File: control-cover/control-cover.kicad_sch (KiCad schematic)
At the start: 9 parts

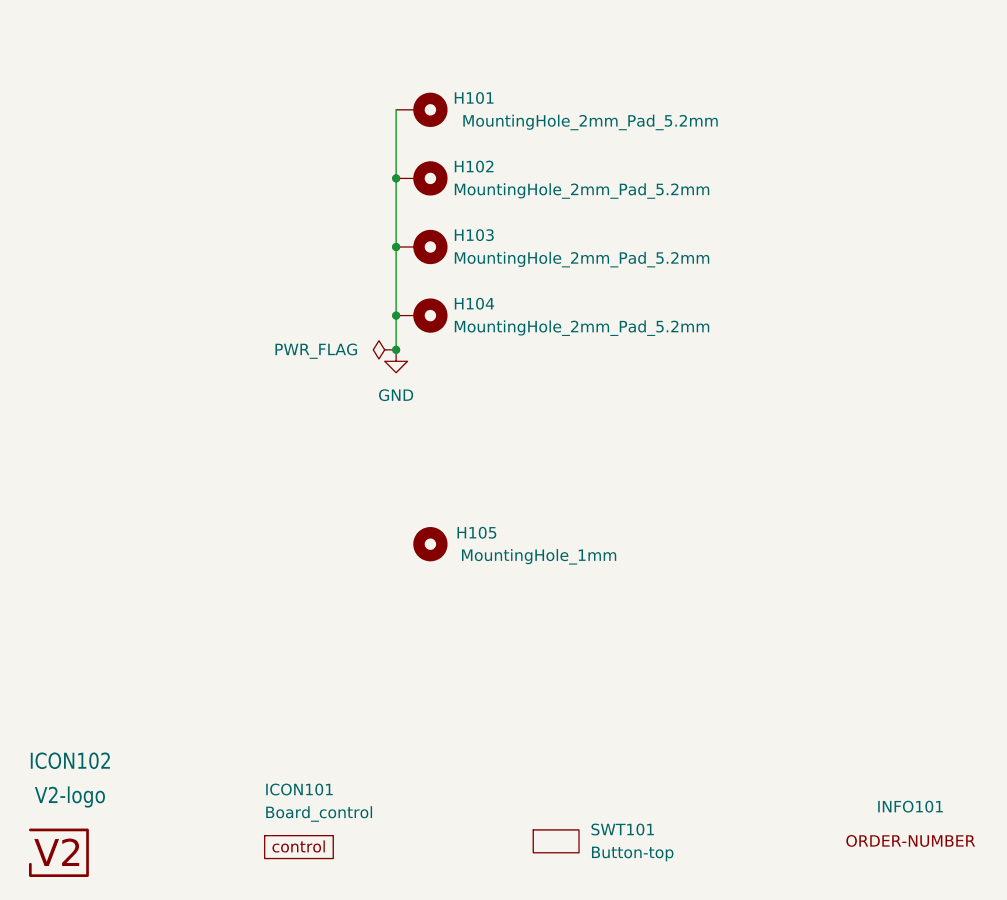
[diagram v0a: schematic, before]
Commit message: Replace Order_Number
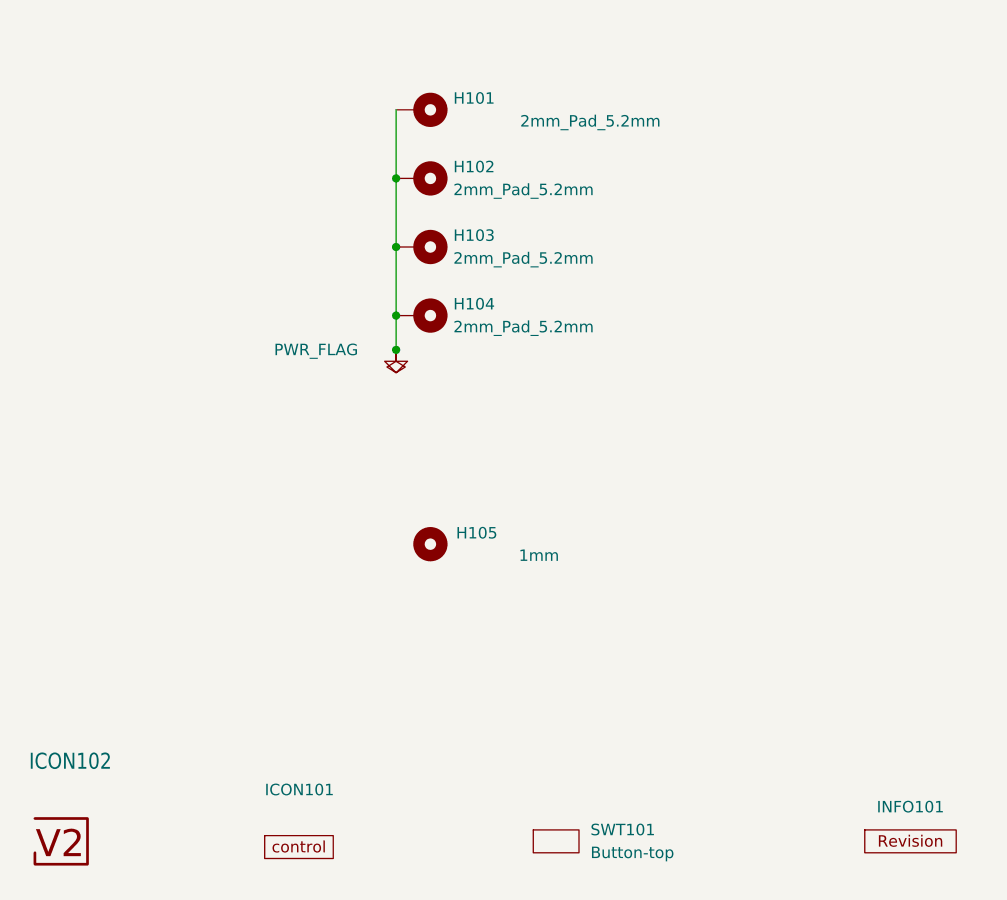
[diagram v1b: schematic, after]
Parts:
- H101, H102, H103, H104: value MountingHole_2mm_Pad_5.2mm -> 2mm_Pad_5.2mm; footprint V2_Mechanical:Mounting_Hole_2mm_Pad_5.2mm -> V2_Mechanical:MountingHole_2mm_Pad_5.2mm; now left out of the parts list
- H105: value MountingHole_1mm -> 1mm; now left out of the parts list
- INFO101: value ORDER-NUMBER -> ~; footprint V2_Production:Order_Number -> V2_Production:Revision; symbol V2_Production:Order_Number -> V2_Production:Revision
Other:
- moved on the sheet: ICON102
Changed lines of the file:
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@@
 (kicad_sch
-	(version 20231120)
+	(version 20250114)
 	(generator "eeschema")
-	(generator_version "8.0")
+	(generator_version "9.0")
 	(paper "A4")
 	(title_block
 		(title "V2 control")
-		(date "2023-01-09")
-		(rev "2")
+		(date "2026-02-13")
+		(rev "2026-02-13")
 		(company "Versio Duo")
 		(comment 1 "cover")
@@
 	)
 	(symbol
-		(lib_id "power:GND")
+		(lib_id "V2_power:GND")
 		(at 138.43 85.09 0)
 		(unit 1)
@@
 					(size 1.27 1.27)
 				)
+				(hide yes)
 			)
 		)
@@
 		(unit 1)
 		(exclude_from_sim no)
-		(in_bom yes)
+		(in_bom no)
 		(on_board yes)
 		(dnp no)
@@
 			)
 		)
-		(property "Value" "MountingHole_2mm_Pad_5.2mm"
+		(property "Value" "2mm_Pad_5.2mm"
 			(at 144.78 67.3099 90)
 			(effects
@@
 			)
 		)
-		(property "Footprint" "V2_Mechanical:Mounting_Hole_2mm_Pad_5.2mm"
+		(property "Footprint" "V2_Mechanical:MountingHole_2mm_Pad_5.2mm"
 			(at 140.97 66.04 0)
 			(effects
@@
 			)
 		)
-		(property "Description" ""
+		(property "Description" "Mounting Hole with connection"
 			(at 140.97 66.04 0)
 			(effects
@@
 	)
 	(symbol
-		(lib_id "V2_Production:Order_Number")
+		(lib_id "V2_Production:Revision")
 		(at 195.58 139.7 0)
 		(unit 1)
@@
 			)
 		)
-		(property "Value" "ORDER-NUMBER"
+		(property "Value" "~"
 			(at 195.58 142.24 0)
 			(effects
@@
 			)
 		)
-		(property "Footprint" "V2_Production:Order_Number"
+		(property "Footprint" "V2_Production:Revision"
 			(at 195.58 144.78 0)
 			(effects
@@
 			)
 		)
+		(property "Sim.Enable" "0"
+			(at 156.21 139.7 0)
+			(effects
+				(font
+					(size 1.27 1.27)
+				)
+				(hide yes)
+			)
+		)
 		(instances
 			(project "control-cover"
@@
 		(unit 1)
 		(exclude_from_sim no)
-		(in_bom yes)
+		(in_bom no)
 		(on_board yes)
 		(dnp no)
@@
 			)
 		)
-		(property "Value" "MountingHole_2mm_Pad_5.2mm"
+		(property "Value" "2mm_Pad_5.2mm"
 			(at 144.78 82.5499 90)
 			(effects
@@
 			)
 		)
-		(property "Footprint" "V2_Mechanical:Mounting_Hole_2mm_Pad_5.2mm"
+		(property "Footprint" "V2_Mechanical:MountingHole_2mm_Pad_5.2mm"
 			(at 140.97 81.28 0)
 			(effects
@@
 			)
 		)
-		(property "Description" ""
+		(property "Description" "Mounting Hole with connection"
 			(at 140.97 81.28 0)
 			(effects
@@
 	)
 	(symbol
-		(lib_name "MountingHole_2mm_Pad_5.2mm_3")
 		(lib_id "V2_Mechanical:MountingHole_2mm_Pad_5.2mm")
 		(at 140.97 58.42 270)
 		(unit 1)
 		(exclude_from_sim no)
-		(in_bom yes)
+		(in_bom no)
 		(on_board yes)
 		(dnp no)
@@
 			)
 		)
-		(property "Value" "MountingHole_2mm_Pad_5.2mm"
+		(property "Value" "2mm_Pad_5.2mm"
 			(at 160.02 59.6899 90)
 			(effects
@@
 			)
 		)
-		(property "Footprint" "V2_Mechanical:Mounting_Hole_2mm_Pad_5.2mm"
+		(property "Footprint" "V2_Mechanical:MountingHole_2mm_Pad_5.2mm"
 			(at 140.97 58.42 0)
 			(effects
@@
 			)
 		)
-		(property "Description" ""
+		(property "Description" "Mounting Hole with connection"
 			(at 140.97 58.42 0)
 			(effects
@@
 				)
 				(justify left)
+				(hide yes)
 			)
 		)
@@
 			)
 		)
+		(property "Sim.Enable" "0"
+			(at 127.635 140.335 0)
+			(effects
+				(font
+					(size 1.27 1.27)
+				)
+				(hide yes)
+			)
+		)
 		(instances
 			(project "control-cover"
@@
 	)
 	(symbol
-		(lib_id "power:PWR_FLAG")
+		(lib_id "V2_power:PWR_FLAG")
 		(at 138.43 85.09 90)
 		(unit 1)
@@
 			)
 		)
-		(property "Datasheet" "~"
+		(property "Datasheet" ""
 			(at 138.43 85.09 0)
 			(effects
@@
 			)
 		)
-		(property "Description" ""
+		(property "Description" "Special symbol for telling ERC where power comes from"
 			(at 138.43 85.09 0)
 			(effects
@@
 		(unit 1)
 		(exclude_from_sim no)
-		(in_bom yes)
+		(in_bom no)
 		(on_board yes)
 		(dnp no)
@@
 			)
 		)
-		(property "Value" "MountingHole_1mm"
+		(property "Value" "1mm"
 			(at 154.305 107.95 0)
 			(effects
@@
 			)
 		)
-		(property "Description" ""
+		(property "Description" "Mounting Hole without connection"
 			(at 142.24 106.68 0)
 			(effects
@@
 					(size 1.778 1.5113)
 				)
+				(hide yes)
 			)
 		)
@@
 		(unit 1)
 		(exclude_from_sim no)
-		(in_bom yes)
+		(in_bom no)
 		(on_board yes)
 		(dnp no)
@@
 			)
 		)
-		(property "Value" "MountingHole_2mm_Pad_5.2mm"
+		(property "Value" "2mm_Pad_5.2mm"
 			(at 144.78 74.9299 90)
 			(effects
@@
 			)
 		)
-		(property "Footprint" "V2_Mechanical:Mounting_Hole_2mm_Pad_5.2mm"
+		(property "Footprint" "V2_Mechanical:MountingHole_2mm_Pad_5.2mm"
 			(at 140.97 73.66 0)
 			(effects
@@
 			)
 		)
-		(property "Description" ""
+		(property "Description" "Mounting Hole with connection"
 			(at 140.97 73.66 0)
 			(effects
@@
 		)
 	)
+	(embedded_fonts no)
 )

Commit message: Update Library
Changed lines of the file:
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@@
-	)
-	(junction
-		(at 138.43 85.09)
-		(diameter 0)
-		(color 0 0 0 0)
 	)
 	(junction
@@
 	(symbol
 		(lib_id "V2_power:GND")
+		(at 149.86 49.53 90)
+		(unit 1)
+		(exclude_from_sim no)
+		(in_bom yes)
+		(on_board yes)
+		(dnp no)
+		(fields_autoplaced yes)
+		(property "Reference" "#PWR0102"
+			(at 156.21 49.53 0)
+			(effects
+				(font
+					(size 1.27 1.27)
+				)
+				(hide yes)
+			)
+		)
+		(property "Value" "GND"
+			(at 154.94 49.53 0)
+			(effects
+				(font
+					(size 1.27 1.27)
+				)
+				(hide yes)
+			)
+		)
+		(property "Footprint" ""
+			(at 149.86 49.53 0)
+			(effects
+				(font
+					(size 1.27 1.27)
+				)
+				(hide yes)
+			)
+		)
+		(property "Datasheet" ""
+			(at 149.86 49.53 0)
+			(effects
+				(font
+					(size 1.27 1.27)
+				)
+				(hide yes)
+			)
+		)
+		(property "Description" ""
+			(at 149.86 49.53 0)
+			(effects
+				(font
+					(size 1.27 1.27)
+				)
+				(hide yes)
+			)
+		)
+		(pin "1"
+		)
+		(instances
+			(project "control-cover"
+				(path "/6c8448b4-b04d-47e1-934e-e40cbe27a7be"
+					(reference "#PWR0102")
+					(unit 1)
+				)
+			)
+		)
+	)
+	(symbol
+		(lib_id "V2_power:GND")
 		(at 138.43 85.09 0)
 		(unit 1)
@@
 		(dnp no)
 		(fields_autoplaced yes)
-		(property "Reference" "#PWR0101"
+		(property "Reference" "#PWR101"
 			(at 138.43 91.44 0)
 			(effects
@@
 			(project "control-cover"
 				(path "/6c8448b4-b04d-47e1-934e-e40cbe27a7be"
-					(reference "#PWR0101")
+					(reference "#PWR101")
 					(unit 1)
 				)
@@
 		)
 		(property "Value" "2mm_Pad_5.2mm"
-			(at 160.02 59.6899 90)
+			(at 153.162 59.4359 90)
 			(effects
 				(font
@@
 	(symbol
 		(lib_id "V2_power:PWR_FLAG")
-		(at 138.43 85.09 90)
+		(at 149.86 49.53 0)
 		(unit 1)
 		(exclude_from_sim no)
@@
 		(on_board yes)
 		(dnp no)
-		(property "Reference" "#FLG0101"
-			(at 136.525 85.09 0)
+		(property "Reference" "#FLG101"
+			(at 149.86 47.625 0)
 			(effects
 				(font
@@
 		)
 		(property "Value" "PWR_FLAG"
-			(at 129.54 85.09 90)
+			(at 139.192 49.53 0)
 			(effects
 				(font
@@
 		)
 		(property "Footprint" ""
-			(at 138.43 85.09 0)
-			(effects
-				(font
-					(size 1.27 1.27)
-				)
-				(hide yes)
-			)
-		)
-		(property "Datasheet" ""
-			(at 138.43 85.09 0)
+			(at 149.86 49.53 0)
+			(effects
+				(font
+					(size 1.27 1.27)
+				)
+				(hide yes)
+			)
+		)
+		(property "Datasheet" ""
+			(at 149.86 49.53 0)
 			(effects
 				(font
@@
 		)
 		(property "Description" "Special symbol for telling ERC where power comes from"
-			(at 138.43 85.09 0)
+			(at 149.86 49.53 0)
 			(effects
 				(font
@@
 			(project "control-cover"
 				(path "/6c8448b4-b04d-47e1-934e-e40cbe27a7be"
-					(reference "#FLG0101")
+					(reference "#FLG101")
 					(unit 1)
 				)
@@
 		)
 		(property "Value" "1mm"
-			(at 154.305 107.95 0)
-			(effects
-				(font
+			(at 147.701 107.95 0)
+			(effects
+				(font
